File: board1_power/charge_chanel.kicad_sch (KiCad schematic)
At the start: 25 parts, among them Q1 SI4920DY, Q2 AO3401A, Q3 AO3401A, Q8 SI4920DY, U3 SY6970QCC, U4 DW01A

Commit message: board1_power: SYS-default channel rework + ESP32-S3 + mux + connectors
Channel (charge_chanel.kicad_sch):
- Reverse-polarity P-FET (DMG2305UX) moved to cell terminal, drain-to-battery;
  charger BAT on CELL_P_PROT, DW01A sense stays on raw CELL_P.
- 0R source selector (R_SYS populated / R_LOAD DNP, both 2010) -> CHn_V_pre,
  PTC relocated after it -> CH_V output. Old Q2/Q3 reverse FETs removed.
- Bootstrap cap 47nF, PMID 6.8uF. Per-cell SK6812 RGB on LED_VDD=CH1_V chain.

Root (board1_power.kicad_sch):
- ESP32-C3 -> ESP32-S3-WROOM-1. SDA=IO8, SCL=IO9, MUX_RST=IO10(+TCA9548A RESET),
  RGB_DATA=IO48 via 330R, USB=IO19/20, boot IO0=pull-up+JP1, heartbeat=IO2.
- Fixed IO45 strapping pin (was tied to +3V3 -> would force 1.8V flash; now NC).
- TCA9548A mux with per-channel I2C (CH1..4_SDA/SCL). 4.7k pull-ups on main bus.
- J2 power 8-pin (CH1..4_V + GND) and J3 signal 4-pin (SDA/SCL/CH_LIVE/SGND),
  both per interconnect.md.

Library: added DMG2305UX (P-FET, SOT-23) to libs/BMS.kicad_sym.

WIP remaining: PWR_FLAGs, no-connect on last RGB DOUT, drop stray CH3_GND label,
cell holders (CELL_P/N left floating by design), optional TPS22917 ESP gate.

Co-Authored-By: Claude Opus 4.8 (1M context) <noreply@anthropic.com>
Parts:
- removed Q2, Q3: AO3401A, Package_TO_SOT_SMD:SOT-23, symbol Transistor_FET:AO3401A
- removed R12, R29: 1M, Resistor_SMD:R_0603_1608Metric, symbol Device:R
- added C11: 0.1uF, Capacitor_SMD:C_0603_1608Metric, symbol Device:C
- added D4: SK6812, LED_SMD:LED_SK6812_PLCC4_5.0x5.0mm_P3.2mm, symbol LED:SK6812
- added Q1: DMG2305UX, Package_TO_SOT_SMD:SOT-23, symbol BMS:DMG2305UX
- added R20, R23: 0R, Resistor_SMD:R_2010_5025Metric, symbol PCM_SparkFun-Resistor:R
- added R22: 100k, PCM_SparkFun-Resistor:R_0603_1608Metric, symbol PCM_SparkFun-Resistor:R
- C12: renamed from C6; value 47uF -> 47nF
- C14: renamed from C4; value 1uF/25V -> 6.8uF/25V
- renumbered C3 to C10, C17 to C13, C5 to C15, C20 to C16, D2 to D3, Q1 to Q2, Q8 to Q2, R6 to R15, R24 to R16, R9 to R17, R26 to R18, R8 to R19, R13 to R21, R31 to R24, U3 to U6, U4 to U7
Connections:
- net CELL_N: now also R22.1
- net CELL_P: now also Q1.3 (D); no longer U6.13 (BAT), U6.14 (BAT)
- net GND: now also C11.1, D4.1 (VSS)
- net CHn_V_pre: now reaches F1.2
- net CHn_V_pre: now also R20.1, R23.1
- net LOAD_P renamed CH_V
- net SYS: no longer names the net of C13.1, L1.2, U6.15 (SYS), U6.16 (SYS)
- net SYS: now also R20.2
- new net: Q1.1 (G), R22.2
- new net CELL_P_PROT: Q1.2 (S), R23.2, U6.13 (BAT), U6.14 (BAT)
- new net LED_VDD: C11.2, D4.3 (VDD)
- new net RGB_DIN: D4.2 (DIN)
- new net RGB_DOUT: D4.4 (DOUT)
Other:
- note removed: "Anti Back Feed"
- note removed: "Reverse Polarity Protection"
- moved on the sheet: F1

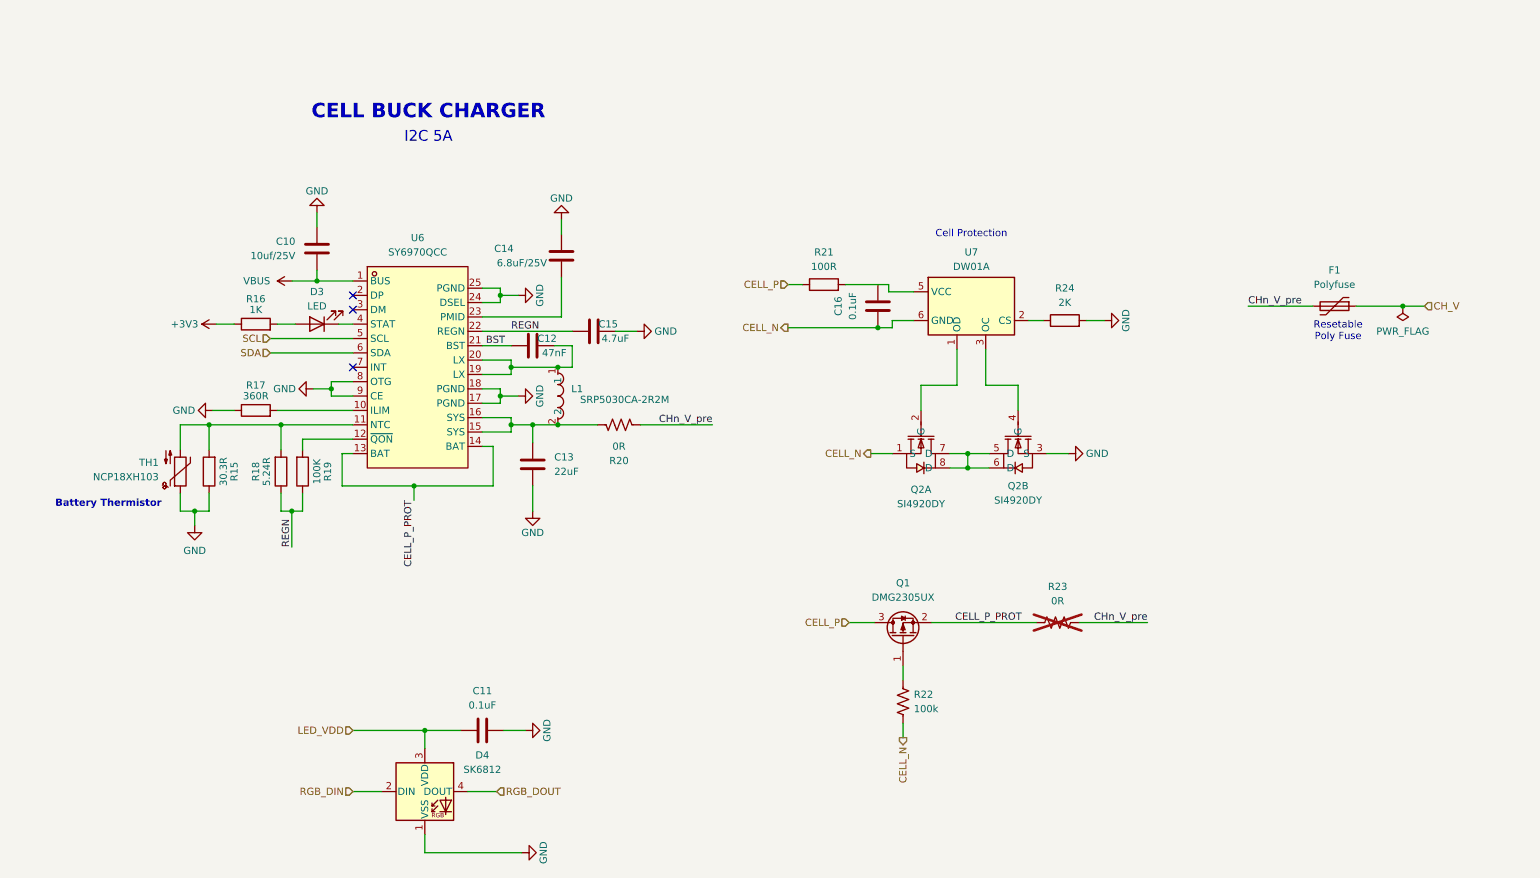
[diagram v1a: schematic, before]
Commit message: board1_power: enable network corrected + all footprints assigned (schematic complete)
- ESP enable rebuilt as a proper diode-OR + shunt:
  * MMBD4448HCQW (D12) quad common-cathode diode-OR -> EN, sources =
    {VBUS divider, CH1_V always-on strap (R59 now 100k), WAKE via 10k, self-hold}
  * R60 100k pull-down on EN (default off)
  * Q9 (2N7002) shunt: Drain->EN, Source->GND, Gate->off-header J4 (CH1_V when in)
  * off-header in -> ESP off (storage); out -> ESP on (launch)
- Assigned footprints to the remaining 26 parts (R/C -> 0603, D1 LED, J2 signal
  connector placeholder); channel-sheet parts apply across all 4 instances.

Remaining ERC items are benign/intentional (Unspecified-pin warnings from imported
symbols, floating cell pins until holder, missing PWR_FLAGs/no-connects).

Co-Authored-By: Claude Opus 4.8 (1M context) <noreply@anthropic.com>
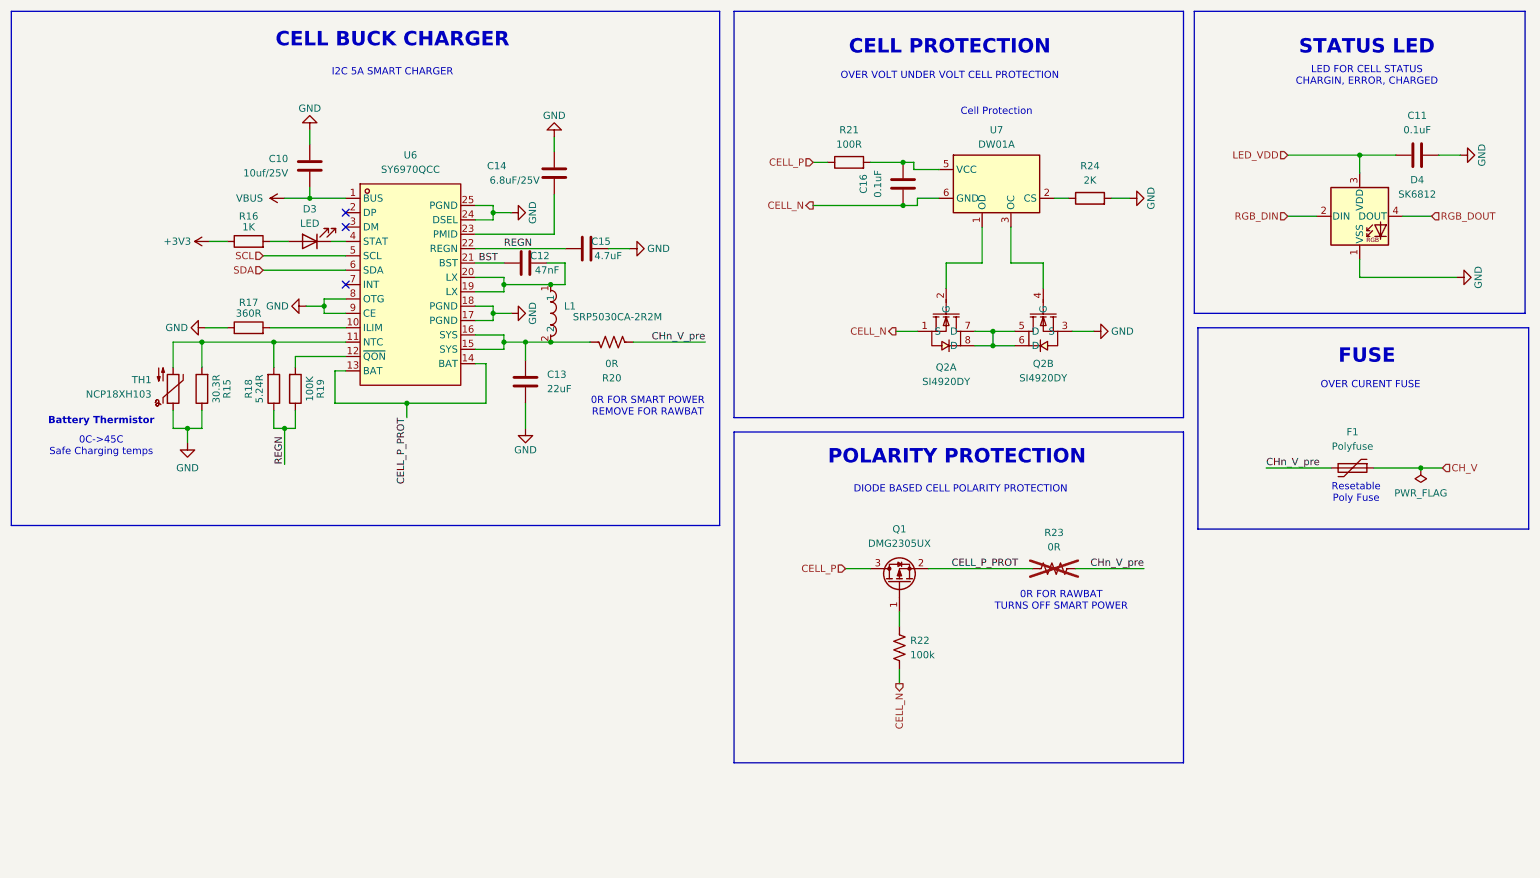
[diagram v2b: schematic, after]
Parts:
- C12: footprint (none) -> Capacitor_SMD:C_0603_1608Metric
- R15, R18, R24: footprint (none) -> Resistor_SMD:R_0603_1608Metric
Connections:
- net at C16.2: now also R21.2, U7.5 (VCC)
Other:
- note added: "0C->45C Safe Charging temps"
- note added: "0R FOR RAWBAT TURNS OFF SMART POWER"
- note added: "0R FOR SMART POWER REMOVE FOR RAWBAT"
- note added: "CELL PROTECTION"
- note added: "DIODE BASED CELL POLARITY PROTECTION"
- note added: "FUSE"
- note added: "I2C 5A SMART CHARGER"
- note added: "LED FOR CELL STATUS CHARGIN, ERROR, CHARGED"
- note added: "OVER CURENT FUSE"
- note added: "OVER VOLT UNDER VOLT CELL PROTECTION"
- note added: "POLARITY PROTECTION"
- note added: "STATUS LED"
- note removed: "I2C 5A"
- moved on the sheet: C10, C11, C12, C13, C14, C15, C16, D3, D4, F1, L1, Q1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

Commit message: board1_power: PCB footprint placement + layout updates
Co-Authored-By: Claude Opus 4.8 (1M context) <noreply@anthropic.com>
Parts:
- C12: footprint Capacitor_SMD:C_0603_1608Metric -> Capacitor_SMD:C_0805_2012Metric
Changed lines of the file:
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@@
 			)
 		)
-		(property "Footprint" "Capacitor_SMD:C_0603_1608Metric"
+		(property "Footprint" "Capacitor_SMD:C_0805_2012Metric"
 			(at 102.235 59.3598 0)
 			(hide yes)
